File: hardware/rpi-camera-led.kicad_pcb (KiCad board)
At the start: 2 copper layers, 25 x 23.9 mm, 24 parts, among them J1 FFC 15P 1.0mm (to Raspberry P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, J2 FFC 15P 1.0mm (to camera), J3 Qwiic (JST SH 1.0mm), J4 SWD program header 2.54mm, Q1 AO3400A, Q2 Phototransistor, U1 CH32V003J4M6

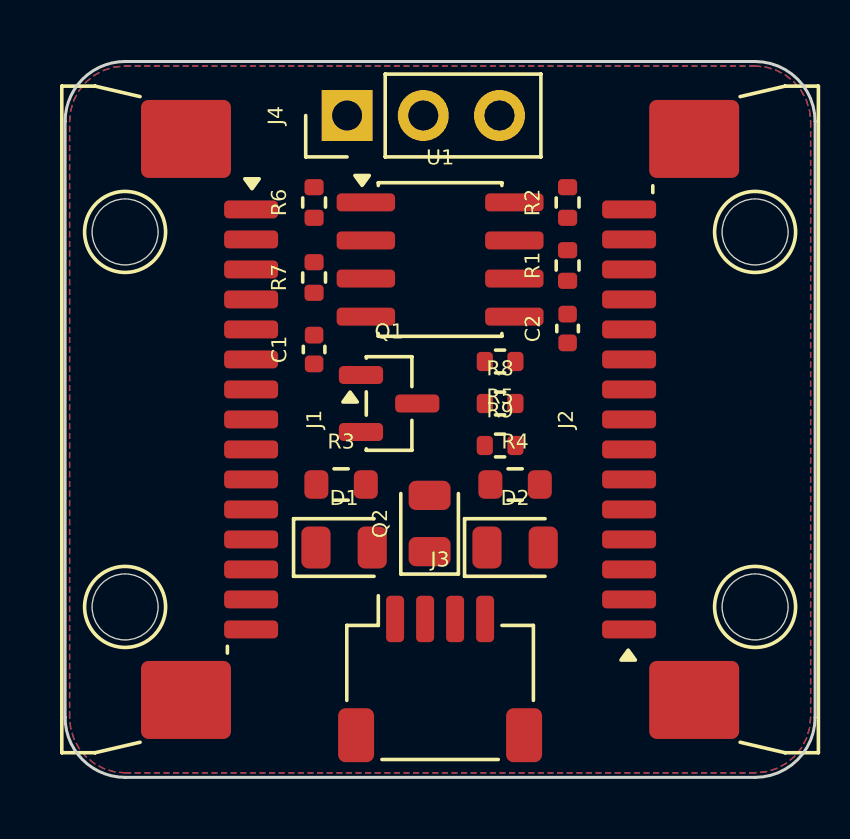
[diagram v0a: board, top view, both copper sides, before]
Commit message: Route the six MIPI pass-through nets in the pcbnew GUI
J1 and J2 face outward on opposite edges, so their contact rows are mirrored
about the board centre and the three differential pairs have to reverse order
between the two connectors.  That reversal is done in the empty pocket under
the J1 housing: each net leaves its pad westward on F.Cu, drops through a via
into a B.Cu channel at its own depth (deeper for a wider span, which keeps the
whole fan planar), runs north/south to its destination row, then crosses the
board on B.Cu and comes back up to the matching J2 pad.

Routed by mouse in pcbnew running on a private Xvfb display; adds
hardware/tools/gui_route.py (xdotool driver, mm->pixel transform measured from
pcbnew's own cursor read-out) and hardware/tools/drc_report.py.

kicad-cli pcb drc --severity-error: 0 violations, 50 unconnected (was 56).

Co-Authored-By: Claude Fable 5 <noreply@anthropic.com>
Claude-Session: https://claude.ai/code/session_01E6VQHygrbAGSqdngQQsBdx
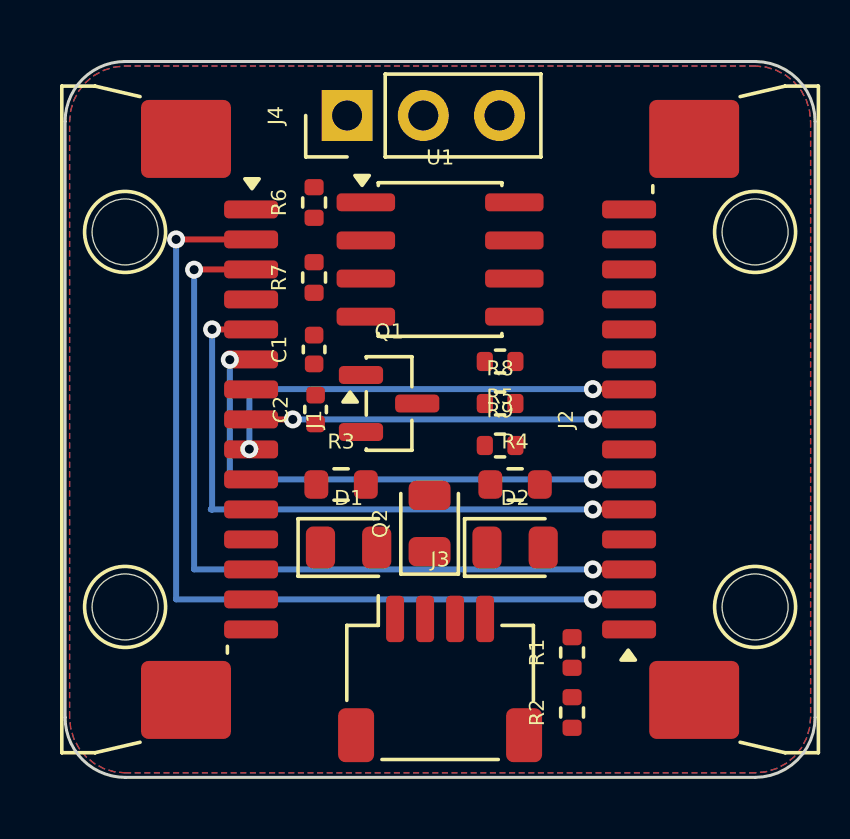
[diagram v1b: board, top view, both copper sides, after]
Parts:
- moved R2 17.0 mm to (36.9, 41.7)
- moved R1 12.9 mm to (36.9, 39.7)
- moved C2 8.82 mm to (28.4, 31.6)
- moved D1 0.15 mm to (29.4, 36.2)
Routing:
- net CAM_D0_N: track 0.00 -> 29.6 mm, vias 0 -> 2
- net CAM_D0_P: track 0.00 -> 26.4 mm, vias 0 -> 2
- net CAM_D1_N: track 0.00 -> 21.3 mm, vias 0 -> 2
- net CAM_D1_P: track 0.00 -> 18.0 mm, vias 0 -> 2
- net CAM_CK_P: track 0.00 -> 14.7 mm, vias 0 -> 2
- net CAM_CK_N: track 0.00 -> 12.6 mm, vias 0 -> 2

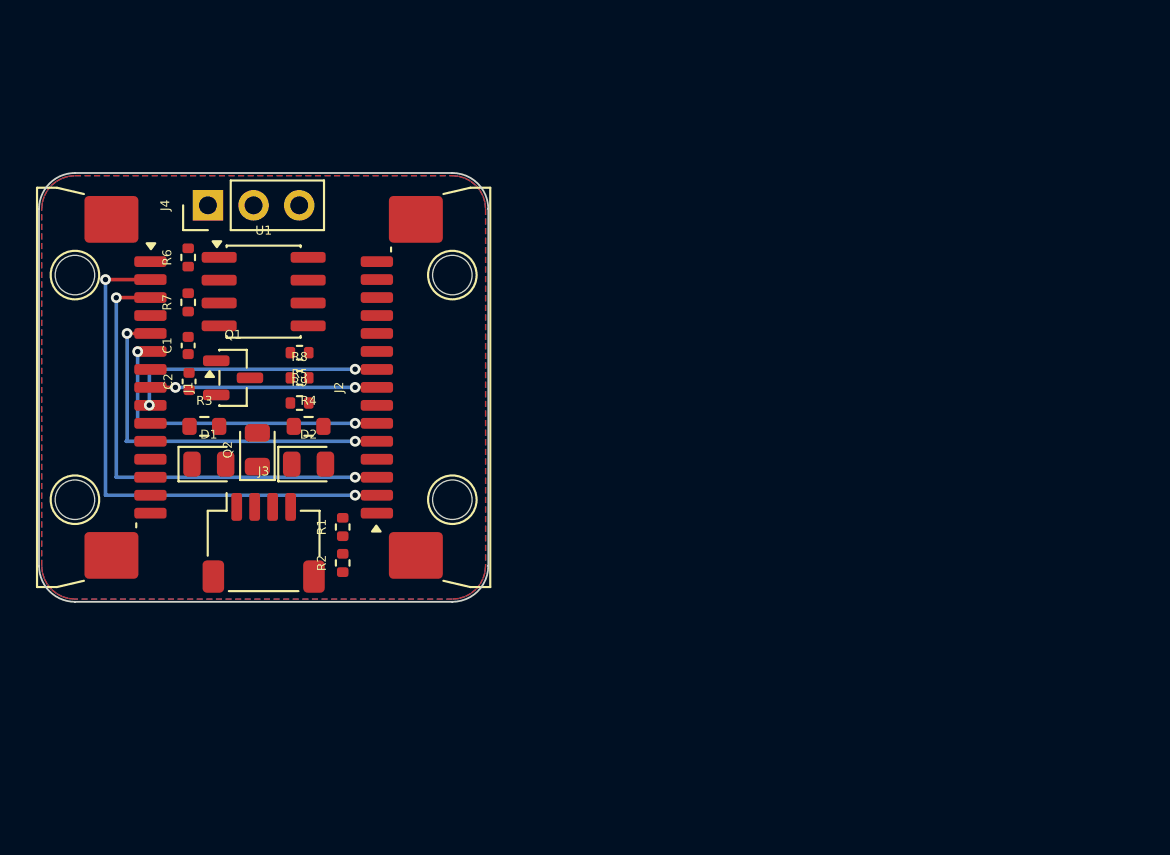
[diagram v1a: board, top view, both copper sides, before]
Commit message: Update the board for the top-contact J2
Bring the PCB in step with the schematic's connector change, and repair
damage the interrupted routing session left in the working file.

J2's footprint becomes rpi-camera-led:JUSHUO_AFA07-S15ECA-00, and both
connectors pick up the Value and MPN text that now names their contact
type.  Nothing else moves: the ECA and FCA land patterns are identical,
so the swap is an identity change only.  The script asserted pad count
and pad geometry were unchanged rather than trusting that, and KiCad's
own DRC now reports schematic_parity: 0.

The working file also carried a duplicate J1 -- two fully net-connected
footprints 0.01mm apart, a stray copy from the session that was cut off
mid-edit.  Removed, keeping the one whose position matches the last
commit.  That leaves 20 footprints for 20 references.

Not repaired here, because it wants a decision rather than a fix: the
36 track segments and 12 vias committed in 351c3b2 are gone from the
working file, so the board is unrouted (50 unconnected).  They are safe
in history if they are wanted back, but they routed the old crossing
arrangement between two bottom-contact connectors -- which is exactly
what this connector change exists to avoid -- so re-routing straight
across looks better than restoring them.

DRC still reports 90 violations, all placement (clearance, mask bridge,
silk).  They are pre-existing: running DRC on the pre-sync board with
only the duplicate removed gives a byte-identical violation set, so
this commit introduced none of them.

Co-Authored-By: Claude Opus 5 (1M context) <noreply@anthropic.com>
Claude-Session: https://claude.ai/code/session_01E6VQHygrbAGSqdngQQsBdx
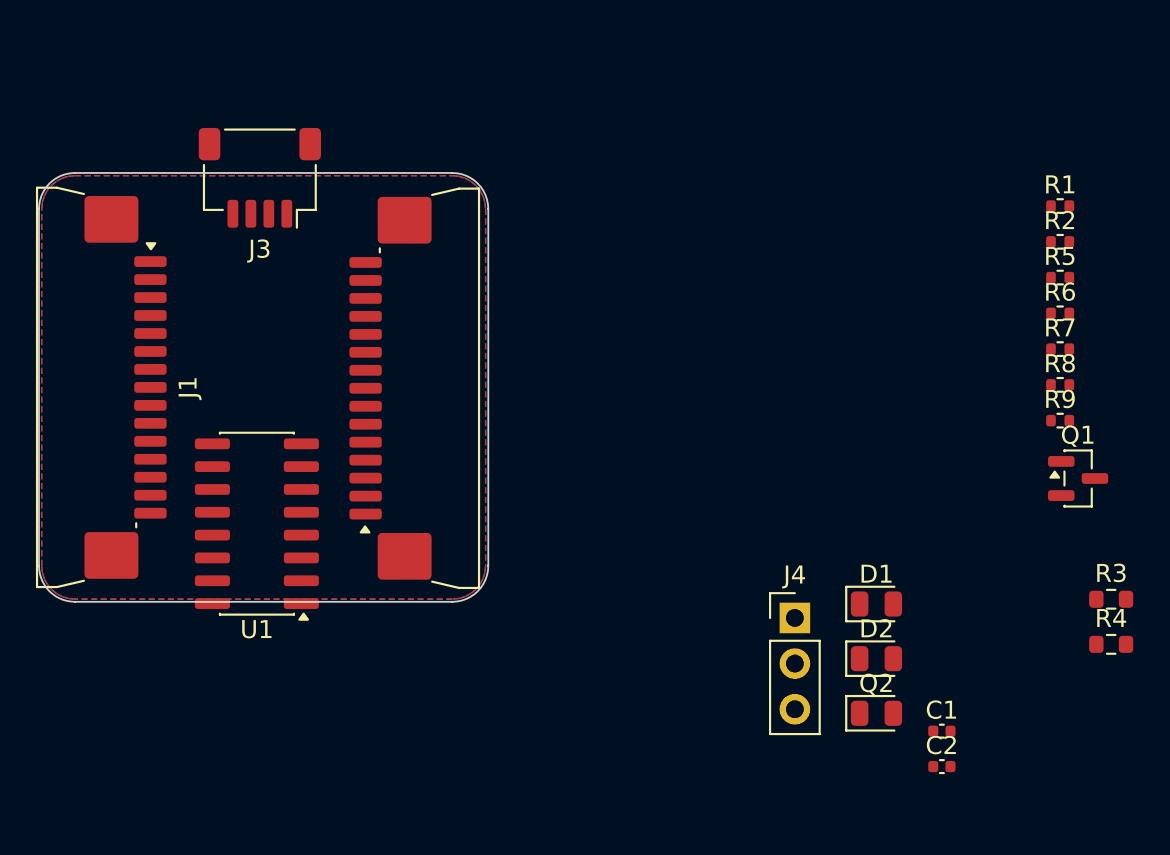
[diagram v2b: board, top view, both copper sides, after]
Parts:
- removed H1, H2, H3, H4: MountingHole_2.2mm, local:MountingHole_2.2mm_M2_NoCourtyard
- C1, C2: footprint C_0402_1005Metric -> Capacitor_SMD:C_0402_1005Metric
- D1, D2, Q2: footprint LED_0805_2012Metric -> LED_SMD:LED_0805_2012Metric
- J1: value FFC 15P 1.0mm (to Raspberry Pi) -> FFC 15P 1.0mm bottom contact (to Raspberry Pi); footprint JUSHUO_AFA07-S15FCA-00_1x15-1MP_P1.0mm_Horizontal -> Connector_FFC-FPC:JUSHUO_AFA07-S15FCA-00_1x15-1MP_P1.0mm_Horizontal
- J2: value FFC 15P 1.0mm (to camera) -> FFC 15P 1.0mm top contact (to camera); footprint JUSHUO_AFA07-S15FCA-00_1x15-1MP_P1.0mm_Horizontal -> rpi-camera-led:JUSHUO_AFA07-S15ECA-00_1x15-1MP_P1.0mm_Horizontal
- J3: footprint JST_SH_SM04B-SRSS-TB_1x04-1MP_P1.00mm_Horizontal -> Connector_JST:JST_SH_SM04B-SRSS-TB_1x04-1MP_P1.00mm_Horizontal
- J4: footprint PinHeader_1x03_P2.54mm_Vertical -> Connector_PinHeader_2.54mm:PinHeader_1x03_P2.54mm_Vertical
- Q1: footprint SOT-23 -> Package_TO_SOT_SMD:SOT-23
- R1, R2, R5, R8, R9: footprint R_0402_1005Metric -> Resistor_SMD:R_0402_1005Metric
- R3, R4: footprint R_0603_1608Metric -> Resistor_SMD:R_0603_1608Metric
- R6, R7: value 10k -> 0; footprint R_0402_1005Metric -> Resistor_SMD:R_0402_1005Metric
- U1: value CH32V003J4M6 -> CH32V003A4M6; footprint SOIC-8_3.9x4.9mm_P1.27mm -> Package_SO:SOIC-16_3.9x9.9mm_P1.27mm
- moved R3 51.4 mm to (79.7, 43.7)
- moved R6 48.6 mm to (76.8, 27.8), turned to 0 degrees
- moved R7 48.6 mm to (76.8, 29.8), turned to 0 degrees
- moved Q1 47.4 mm to (77.8, 37.0)
- moved C1 47.1 mm to (70.2, 51.1), turned to 0 degrees
- moved C2 47.1 mm to (70.2, 53.0), turned to 0 degrees
- moved R4 46.3 mm to (79.7, 46.2)
- moved R2 43.7 mm to (76.8, 23.8), turned to 0 degrees
- moved R1 43.7 mm to (76.8, 21.8), turned to 0 degrees
- moved R5 42.5 mm to (76.8, 25.8), turned to 0 degrees
- moved R9 42.3 mm to (76.8, 33.8)
- moved R8 42.3 mm to (76.8, 31.8)
- moved J4 39.9 mm to (62.1, 44.8), turned to 0 degrees
- moved D1 38.0 mm to (66.6, 44.0)
- moved Q2 37.4 mm to (66.6, 50.1), turned to 0 degrees
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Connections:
- R5 pad 1: SWIO -> LED_PWM
- U1 pad 1: CAM_IO0 -> SDA
- U1 pad 2: GND -> SCL
- U1 pad 3: CAM_IO1 -> LED_PWM
- U1 pad 4: 3V3 -> LIGHT_SENSE
- U1 pad 5: SDA -> unconnected-(U1-PC6-Pad5)
- U1 pad 6: SCL -> unconnected-(U1-PC7-Pad6)
- U1 pad 7: LIGHT_SENSE -> SWIO
- U1 pad 8: SWIO -> unconnected-(U1-PD4-Pad8)
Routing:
- net CAM_D0_N: track 29.6 -> 0.00 mm, vias 2 -> 0
- net CAM_D0_P: track 26.4 -> 0.00 mm, vias 2 -> 0
- net CAM_D1_N: track 21.3 -> 0.00 mm, vias 2 -> 0
- net CAM_D1_P: track 18.0 -> 0.00 mm, vias 2 -> 0
- net CAM_CK_P: track 14.7 -> 0.00 mm, vias 2 -> 0
- net CAM_CK_N: track 12.6 -> 0.00 mm, vias 2 -> 0

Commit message: Actually reverse J2's pin order, which a708eef only implied
a708eef swapped J2 to the top-contact part and claimed that made the
bus route straight.  It did not.  The two variants share one land
pattern, so changing the part moved no pad and altered no net: the
board was byte-identical in every way that matters and every
pass-through net still had to cross the bus.  Tim spotted it -- the
connector did not seem to have changed because nothing had.

The reversal has to live in the net mapping, and now does.  Measured
from the board rather than assumed: J1 sits at -90 degrees and J2 at
+90, so J1 pad k is physically opposite J2 pad 16-k (J1.1 faces J2.15,
J1.8 faces J2.8, dy 0.049mm).  A net can only be a straight trace if it
joins such a pair.

Dropping (mirror x) from J2's symbol does exactly that and nothing
else: the pin numbering reverses against labels and wires that all stay
where they are, so J2.m now carries what J1.(16-m) does.  That is also
what the top-contact part buys -- its cable goes in flipped, so contact
m really does land on the conductor the Pi calls 16-m.  The two changes
are one change; a708eef was half of it.

On the sheet the two connectors' pin numbers now run in opposite
directions, which is the honest picture: every net's label lines up
horizontally across the gap.

check_schematic.py gains that as a standing invariant rather than a
one-off measurement -- it now fails any net where J1.k does not face
J2.(16-k), the GPIO channels pairing through R6/R7 by name.  Checked
against the pre-fix schematic, where it flags 14 of the 15 nets (pin 8
is self-symmetric), so it is not vacuous.

The board's J2 pads follow, 14 reassigned, pad 8 unchanged for the same
reason.  No pad moved; kicad-cli reports schematic_parity 0.  DRC goes
90 -> 92 violations, the delta being two more starved_thermal: GND now
lands on J2 pads 6/9/12/15 instead of 1/4/7/10, so the zone's thermal
spokes fall differently.  Clearance and mask-bridge counts are
unchanged, and all of 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
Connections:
- J2 pad 1: GND -> 3V3
- J2 pad 10: GND -> CAM_D1_P
- J2 pad 11: CAM_IO0 -> CAM_D1_N
- J2 pad 12: CAM_IO1 -> GND
- J2 pad 13: SCL -> CAM_D0_P
- J2 pad 14: SDA -> CAM_D0_N
- J2 pad 15: 3V3 -> GND
- J2 pad 2: CAM_D0_N -> SDA
- J2 pad 3: CAM_D0_P -> SCL
- J2 pad 4: GND -> CAM_IO1
- J2 pad 5: CAM_D1_N -> CAM_IO0
- J2 pad 6: CAM_D1_P -> GND
- J2 pad 7: GND -> CAM_CK_P
- J2 pad 9: CAM_CK_P -> GND
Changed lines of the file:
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@@
 			(layers "F.Cu" "F.Mask" "F.Paste")
 			(roundrect_rratio 0.25)
-			(net 10 "GND")
+			(net 1 "3V3")
 			(pinfunction "Pin_1")
 			(pintype "passive")
@@
 			(layers "F.Cu" "F.Mask" "F.Paste")
 			(roundrect_rratio 0.25)
-			(net 4 "CAM_D0_N")
+			(net 19 "SDA")
 			(pinfunction "Pin_2")
 			(pintype "passive")
@@
 			(layers "F.Cu" "F.Mask" "F.Paste")
 			(roundrect_rratio 0.25)
-			(net 5 "CAM_D0_P")
+			(net 18 "SCL")
 			(pinfunction "Pin_3")
 			(pintype "passive")
@@
 			(layers "F.Cu" "F.Mask" "F.Paste")
 			(roundrect_rratio 0.25)
-			(net 10 "GND")
+			(net 9 "CAM_IO1")
 			(pinfunction "Pin_4")
 			(pintype "passive")
@@
 			(layers "F.Cu" "F.Mask" "F.Paste")
 			(roundrect_rratio 0.25)
-			(net 6 "CAM_D1_N")
+			(net 8 "CAM_IO0")
 			(pinfunction "Pin_5")
 			(pintype "passive")
@@
 			(layers "F.Cu" "F.Mask" "F.Paste")
 			(roundrect_rratio 0.25)
-			(net 7 "CAM_D1_P")
+			(net 10 "GND")
 			(pinfunction "Pin_6")
 			(pintype "passive")
@@
 			(layers "F.Cu" "F.Mask" "F.Paste")
 			(roundrect_rratio 0.25)
-			(net 10 "GND")
+			(net 3 "CAM_CK_P")
 			(pinfunction "Pin_7")
 			(pintype "passive")
@@
 			(layers "F.Cu" "F.Mask" "F.Paste")
 			(roundrect_rratio 0.25)
-			(net 3 "CAM_CK_P")
+			(net 10 "GND")
 			(pinfunction "Pin_9")
 			(pintype "passive")
@@
 			(layers "F.Cu" "F.Mask" "F.Paste")
 			(roundrect_rratio 0.25)
-			(net 10 "GND")
+			(net 7 "CAM_D1_P")
 			(pinfunction "Pin_10")
 			(pintype "passive")
@@
 			(layers "F.Cu" "F.Mask" "F.Paste")
 			(roundrect_rratio 0.25)
-			(net 8 "CAM_IO0")
+			(net 6 "CAM_D1_N")
 			(pinfunction "Pin_11")
 			(pintype "passive")
@@
 			(layers "F.Cu" "F.Mask" "F.Paste")
 			(roundrect_rratio 0.25)
-			(net 9 "CAM_IO1")
+			(net 10 "GND")
 			(pinfunction "Pin_12")
 			(pintype "passive")
@@
 			(layers "F.Cu" "F.Mask" "F.Paste")
 			(roundrect_rratio 0.25)
-			(net 18 "SCL")
+			(net 5 "CAM_D0_P")
 			(pinfunction "Pin_13")
 			(pintype "passive")
@@
 			(layers "F.Cu" "F.Mask" "F.Paste")
 			(roundrect_rratio 0.25)
-			(net 19 "SDA")
+			(net 4 "CAM_D0_N")
 			(pinfunction "Pin_14")
 			(pintype "passive")
@@
 			(layers "F.Cu" "F.Mask" "F.Paste")
 			(roundrect_rratio 0.25)
-			(net 1 "3V3")
+			(net 10 "GND")
 			(pinfunction "Pin_15")
 			(pintype "passive")
